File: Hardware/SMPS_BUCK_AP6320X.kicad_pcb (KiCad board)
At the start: 2 copper layers, 14.4 x 15.4 mm, 22 parts, among them J1 61300411121, U1 AP63205WU-7

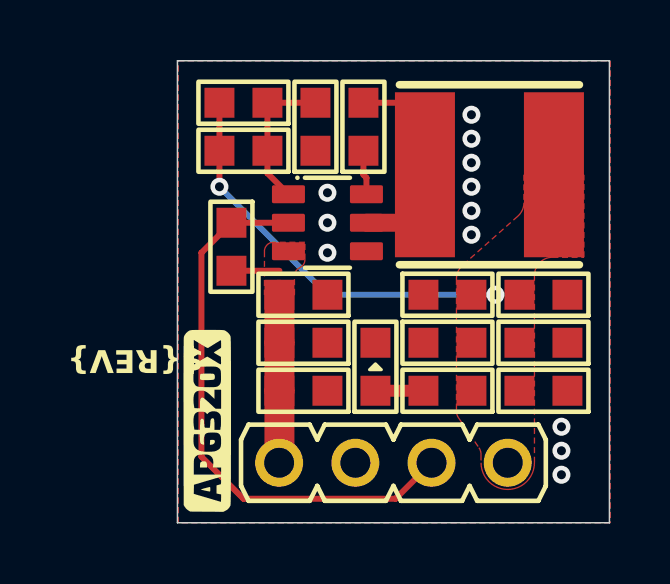
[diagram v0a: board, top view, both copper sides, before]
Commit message: Files are now placed into folders.
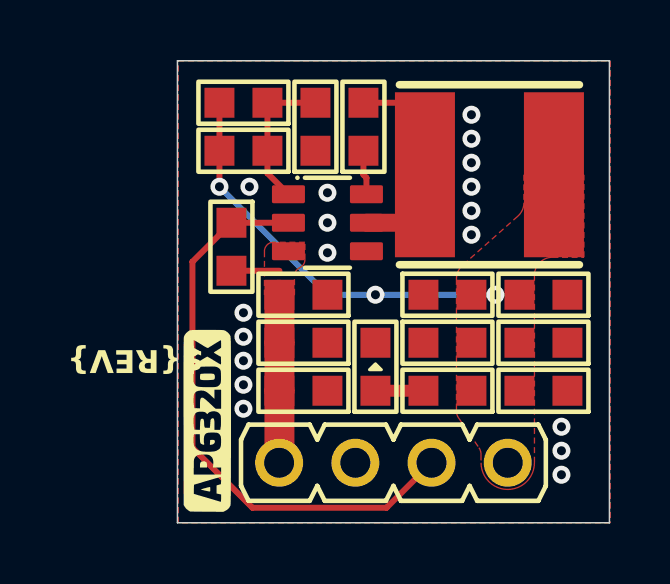
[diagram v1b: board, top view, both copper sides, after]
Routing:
- net GND: vias 12 -> 18
- net /VOUT: vias 2 -> 3
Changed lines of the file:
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@@
+	)
+	(via
+		(at 150.2 119.6)
+		(size 0.6)
+		(drill 0.3)
+		(layers "F.Cu" "B.Cu")
+		(net 2)
+	)
+	(via
+		(at 150.2 121.2)
+		(size 0.6)
+		(drill 0.3)
+		(layers "F.Cu" "B.Cu")
+		(net 2)
 	)
 	(via
@@
 	)
 	(via
+		(at 150.2 120.4)
+		(size 0.6)
+		(drill 0.3)
+		(layers "F.Cu" "B.Cu")
+		(net 2)
+	)
+	(via
 		(at 157.8 114.6)
 		(size 0.6)
@@
 	)
 	(via
+		(at 150.2 118)
+		(size 0.6)
+		(drill 0.3)
+		(layers "F.Cu" "B.Cu")
+		(net 2)
+	)
+	(via
 		(at 160.8 123.4)
 		(size 0.6)
@@
 	)
 	(via
+		(at 150.2 118.8)
+		(size 0.6)
+		(drill 0.3)
+		(layers "F.Cu" "B.Cu")
+		(net 2)
+	)
+	(via
 		(at 160.8 121.8)
+		(size 0.6)
+		(drill 0.3)
+		(layers "F.Cu" "B.Cu")
+		(net 2)
+	)
+	(via
+		(at 150.4 113.8)
 		(size 0.6)
 		(drill 0.3)
@@
 	)
 	(via
+		(at 154.6 117.4)
+		(size 0.6)
+		(drill 0.3)
+		(layers "F.Cu" "B.Cu")
+		(net 7)
+	)
+	(via
 		(at 149.4 113.8)
 		(size 0.6)
@@
 	)
 	(segment
-		(start 149.8 115)
-		(end 148.8 116)
-		(width 0.2)
-		(layer "F.Cu")
-		(net 8)
-	)
-	(segment
-		(start 148.8 122.8)
-		(end 148.8 116)
+		(start 150.5 124.5)
+		(end 148.5 122.5)
+		(width 0.2)
+		(layer "F.Cu")
+		(net 8)
+	)
+	(segment
+		(start 148.5 116.3)
+		(end 149.8 115)
 		(width 0.2)
 		(layer "F.Cu")
@@
 	)
 	(segment
-		(start 155.27 124.2)
-		(end 150.2 124.2)
+		(start 148.5 122.5)
+		(end 148.5 116.3)
 		(width 0.2)
 		(layer "F.Cu")
@@
 	(segment
 		(start 156.47 123)
-		(end 155.27 124.2)
-		(width 0.2)
-		(layer "F.Cu")
-		(net 8)
-	)
-	(segment
-		(start 150.2 124.2)
-		(end 148.8 122.8)
+		(end 154.97 124.5)
+		(width 0.2)
+		(layer "F.Cu")
+		(net 8)
+	)
+	(segment
+		(start 154.97 124.5)
+		(end 150.5 124.5)
 		(width 0.2)
 		(layer "F.Cu")
@@
 		(min_thickness 0.25)
 		(filled_areas_thickness no)
-		(fill
+		(fill yes
 			(thermal_gap 0.5)
 			(thermal_bridge_width 0.5)

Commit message: Added BOM files, 3D and unit prices to BOM.
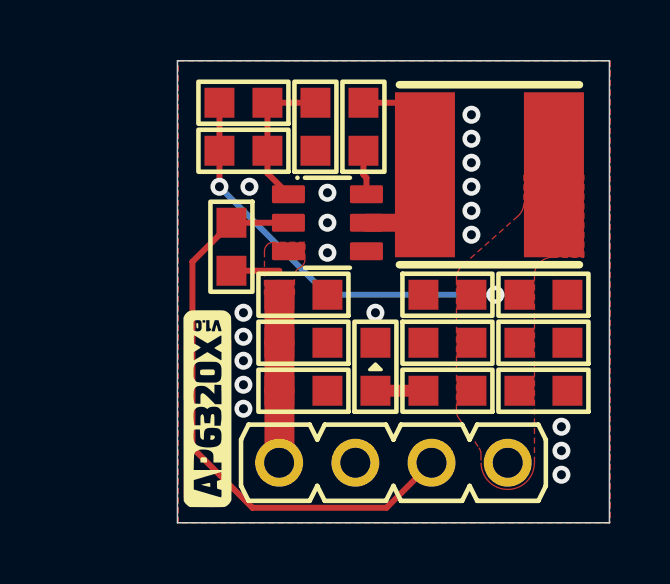
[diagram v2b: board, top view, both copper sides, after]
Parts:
- L1: value Abracon LLC ASPI-0628-6R8M-T1 -> Abracon LLC ASPI-6045S-6R8M-T; footprint kicad_lib:Abracon_LLC_ASPI-0628-6R8M-T1 -> kicad_lib:Abracon_LLC_ASPI-6045S-6R8M-T
- moved G*** 10.6 mm to (160.6, 114.2), turned to 180 degrees
- moved G*** 10.6 mm to (160.6, 111.4), turned to 180 degrees
- moved REF** 3.80 mm to (155.0, 112.2), turned to 180 degrees
- moved G*** 0.40 mm to (149.0, 121.2)
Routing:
- net GND: vias 18 -> 19
- net /VOUT: vias 3 -> 2
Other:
- board text removed: "${REV}"
